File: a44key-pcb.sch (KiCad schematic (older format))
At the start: 60 parts

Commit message: Submodules added
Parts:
- C1, C2, C3, C4, C5, C6, C7: renamed from C?; footprint (none) -> Capacitor_SMD:C_0805_2012Metric
- D1, D10, D11, D12, D13, D14, D15, D16, D17, D18, D19, D2, D20, D21, D22, D3, D4, D5, D6, D7, D8, D9: renamed from D?; footprint (none) -> MX_Alps_Hybrid:MX-1U-NoLED
- F1: renamed from F?; footprint (none) -> MX_Alps_Hybrid:MX-1U-NoLED
- MX1, MX10, MX11, MX12, MX13, MX14, MX15, MX16, MX17, MX18, MX19, MX2, MX20, MX21, MX22, MX3, MX4, MX5, MX6, MX7, MX8, MX9: renamed from MX?; footprint (none) -> MX_Alps_Hybrid:MX-1U-NoLED
- R1, R2, R3, R4: renamed from R?; footprint (none) -> Resistor_SMD:R_0805_2012Metric
- SW1: renamed from SW?; footprint (none) -> random-keyboard-parts:SKQG-1155865
- USB1: renamed from USB?; footprint (none) -> random-keyboard-parts:Molex-0548190589
- Y1: renamed from Y?; footprint (none) -> Crystal:Crystal_SMD_3225-4Pin_3.2x2.5mm_HandSoldering
- gave numbers to parts that had none: 1

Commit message: Submodules added
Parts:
- added J1: AudioJack3, Connector_Audio:Jack_3.5mm_CUI_SJ1-3535NG_Horizontal, symbol Connector:AudioJack3
- D1, D10, D11, D12, D13, D14, D15, D16, D17, D18, D19, D2, D20, D21, D22, D3, D4, D5, D6, D7, D8, D9: footprint MX_Alps_Hybrid:MX-1U-NoLED -> Diode_SMD:D_SOD-123
- F1: footprint MX_Alps_Hybrid:MX-1U-NoLED -> Fuse:Fuse_1206_3216Metric
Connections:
- net GND: now also U1.15 (GND), U1.23 (GND), U1.35 (GND), U1.43 (GND)
- new net R: J1.R
- new net S: J1.S
- new net T: J1.T
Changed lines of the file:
@@
 F 0 "F1" V 6075 1200 50  0000 C CNN
 F 1 "Polyfuse" V 6166 1200 50  0000 C CNN
-F 2 "MX_Alps_Hybrid:MX-1U-NoLED" H 6350 1000 50  0001 L CNN
+F 2 "Fuse:Fuse_1206_3216Metric" H 6350 1000 50  0001 L CNN
 F 3 "~" H 6300 1200 50  0001 C CNN
 	1    6300 1200
@@
 F 0 "D1" V 6596 2532 50  0000 R CNN
 F 1 "D_Small" V 6505 2532 50  0000 R CNN
-F 2 "MX_Alps_Hybrid:MX-1U-NoLED" V 6550 2600 50  0001 C CNN
+F 2 "Diode_SMD:D_SOD-123" V 6550 2600 50  0001 C CNN
 F 3 "~" V 6550 2600 50  0001 C CNN
 	1    6550 2600
@@
 F 0 "D5" V 7296 2532 50  0000 R CNN
 F 1 "D_Small" V 7205 2532 50  0000 R CNN
-F 2 "MX_Alps_Hybrid:MX-1U-NoLED" V 7250 2600 50  0001 C CNN
+F 2 "Diode_SMD:D_SOD-123" V 7250 2600 50  0001 C CNN
 F 3 "~" V 7250 2600 50  0001 C CNN
 	1    7250 2600
@@
 F 0 "D2" V 6596 3332 50  0000 R CNN
 F 1 "D_Small" V 6505 3332 50  0000 R CNN
-F 2 "MX_Alps_Hybrid:MX-1U-NoLED" V 6550 3400 50  0001 C CNN
+F 2 "Diode_SMD:D_SOD-123" V 6550 3400 50  0001 C CNN
 F 3 "~" V 6550 3400 50  0001 C CNN
 	1    6550 3400
@@
 F 0 "D6" V 7296 3332 50  0000 R CNN
 F 1 "D_Small" V 7205 3332 50  0000 R CNN
-F 2 "MX_Alps_Hybrid:MX-1U-NoLED" V 7250 3400 50  0001 C CNN
+F 2 "Diode_SMD:D_SOD-123" V 7250 3400 50  0001 C CNN
 F 3 "~" V 7250 3400 50  0001 C CNN
 	1    7250 3400
@@
 F 0 "D9" V 7996 2532 50  0000 R CNN
 F 1 "D_Small" V 7905 2532 50  0000 R CNN
-F 2 "MX_Alps_Hybrid:MX-1U-NoLED" V 7950 2600 50  0001 C CNN
+F 2 "Diode_SMD:D_SOD-123" V 7950 2600 50  0001 C CNN
 F 3 "~" V 7950 2600 50  0001 C CNN
 	1    7950 2600
@@
 F 0 "D13" V 8696 2532 50  0000 R CNN
 F 1 "D_Small" V 8605 2532 50  0000 R CNN
-F 2 "MX_Alps_Hybrid:MX-1U-NoLED" V 8650 2600 50  0001 C CNN
+F 2 "Diode_SMD:D_SOD-123" V 8650 2600 50  0001 C CNN
 F 3 "~" V 8650 2600 50  0001 C CNN
 	1    8650 2600
@@
 F 0 "D10" V 7996 3332 50  0000 R CNN
 F 1 "D_Small" V 7905 3332 50  0000 R CNN
-F 2 "MX_Alps_Hybrid:MX-1U-NoLED" V 7950 3400 50  0001 C CNN
+F 2 "Diode_SMD:D_SOD-123" V 7950 3400 50  0001 C CNN
 F 3 "~" V 7950 3400 50  0001 C CNN
 	1    7950 3400
@@
 F 0 "D14" V 8696 3332 50  0000 R CNN
 F 1 "D_Small" V 8605 3332 50  0000 R CNN
-F 2 "MX_Alps_Hybrid:MX-1U-NoLED" V 8650 3400 50  0001 C CNN
+F 2 "Diode_SMD:D_SOD-123" V 8650 3400 50  0001 C CNN
 F 3 "~" V 8650 3400 50  0001 C CNN
 	1    8650 3400
@@
 F 0 "D3" V 6596 4132 50  0000 R CNN
 F 1 "D_Small" V 6505 4132 50  0000 R CNN
-F 2 "MX_Alps_Hybrid:MX-1U-NoLED" V 6550 4200 50  0001 C CNN
+F 2 "Diode_SMD:D_SOD-123" V 6550 4200 50  0001 C CNN
 F 3 "~" V 6550 4200 50  0001 C CNN
 	1    6550 4200
@@
 F 0 "D7" V 7296 4132 50  0000 R CNN
 F 1 "D_Small" V 7205 4132 50  0000 R CNN
-F 2 "MX_Alps_Hybrid:MX-1U-NoLED" V 7250 4200 50  0001 C CNN
+F 2 "Diode_SMD:D_SOD-123" V 7250 4200 50  0001 C CNN
 F 3 "~" V 7250 4200 50  0001 C CNN
 	1    7250 4200
@@
 F 0 "D4" V 6596 4932 50  0000 R CNN
 F 1 "D_Small" V 6505 4932 50  0000 R CNN
-F 2 "MX_Alps_Hybrid:MX-1U-NoLED" V 6550 5000 50  0001 C CNN
+F 2 "Diode_SMD:D_SOD-123" V 6550 5000 50  0001 C CNN
 F 3 "~" V 6550 5000 50  0001 C CNN
 	1    6550 5000
@@
 F 0 "D8" V 7296 4932 50  0000 R CNN
 F 1 "D_Small" V 7205 4932 50  0000 R CNN
-F 2 "MX_Alps_Hybrid:MX-1U-NoLED" V 7250 5000 50  0001 C CNN
+F 2 "Diode_SMD:D_SOD-123" V 7250 5000 50  0001 C CNN
 F 3 "~" V 7250 5000 50  0001 C CNN
 	1    7250 5000
@@
 F 0 "D11" V 7996 4132 50  0000 R CNN
 F 1 "D_Small" V 7905 4132 50  0000 R CNN
-F 2 "MX_Alps_Hybrid:MX-1U-NoLED" V 7950 4200 50  0001 C CNN
+F 2 "Diode_SMD:D_SOD-123" V 7950 4200 50  0001 C CNN
 F 3 "~" V 7950 4200 50  0001 C CNN
 	1    7950 4200
@@
 F 0 "D15" V 8696 4132 50  0000 R CNN
 F 1 "D_Small" V 8605 4132 50  0000 R CNN
-F 2 "MX_Alps_Hybrid:MX-1U-NoLED" V 8650 4200 50  0001 C CNN
+F 2 "Diode_SMD:D_SOD-123" V 8650 4200 50  0001 C CNN
 F 3 "~" V 8650 4200 50  0001 C CNN
 	1    8650 4200
@@
 F 0 "D12" V 7996 4932 50  0000 R CNN
 F 1 "D_Small" V 7905 4932 50  0000 R CNN
-F 2 "MX_Alps_Hybrid:MX-1U-NoLED" V 7950 5000 50  0001 C CNN
+F 2 "Diode_SMD:D_SOD-123" V 7950 5000 50  0001 C CNN
 F 3 "~" V 7950 5000 50  0001 C CNN
 	1    7950 5000
@@
 F 0 "D16" V 8696 4932 50  0000 R CNN
 F 1 "D_Small" V 8605 4932 50  0000 R CNN
-F 2 "MX_Alps_Hybrid:MX-1U-NoLED" V 8650 5000 50  0001 C CNN
+F 2 "Diode_SMD:D_SOD-123" V 8650 5000 50  0001 C CNN
 F 3 "~" V 8650 5000 50  0001 C CNN
 	1    8650 5000
@@
 F 0 "D17" V 9346 2532 50  0000 R CNN
 F 1 "D_Small" V 9255 2532 50  0000 R CNN
-F 2 "MX_Alps_Hybrid:MX-1U-NoLED" V 9300 2600 50  0001 C CNN
+F 2 "Diode_SMD:D_SOD-123" V 9300 2600 50  0001 C CNN
 F 3 "~" V 9300 2600 50  0001 C CNN
 	1    9300 2600
@@
 F 0 "D20" V 10046 2532 50  0000 R CNN
 F 1 "D_Small" V 9955 2532 50  0000 R CNN
-F 2 "MX_Alps_Hybrid:MX-1U-NoLED" V 10000 2600 50  0001 C CNN
+F 2 "Diode_SMD:D_SOD-123" V 10000 2600 50  0001 C CNN
 F 3 "~" V 10000 2600 50  0001 C CNN
 	1    10000 2600
@@
 F 0 "D18" V 9346 3332 50  0000 R CNN
 F 1 "D_Small" V 9255 3332 50  0000 R CNN
-F 2 "MX_Alps_Hybrid:MX-1U-NoLED" V 9300 3400 50  0001 C CNN
+F 2 "Diode_SMD:D_SOD-123" V 9300 3400 50  0001 C CNN
 F 3 "~" V 9300 3400 50  0001 C CNN
 	1    9300 3400
@@
 F 0 "D21" V 10046 3332 50  0000 R CNN
 F 1 "D_Small" V 9955 3332 50  0000 R CNN
-F 2 "MX_Alps_Hybrid:MX-1U-NoLED" V 10000 3400 50  0001 C CNN
+F 2 "Diode_SMD:D_SOD-123" V 10000 3400 50  0001 C CNN
 F 3 "~" V 10000 3400 50  0001 C CNN
 	1    10000 3400
@@
 F 0 "D19" V 9346 4132 50  0000 R CNN
 F 1 "D_Small" V 9255 4132 50  0000 R CNN
-F 2 "MX_Alps_Hybrid:MX-1U-NoLED" V 9300 4200 50  0001 C CNN
+F 2 "Diode_SMD:D_SOD-123" V 9300 4200 50  0001 C CNN
 F 3 "~" V 9300 4200 50  0001 C CNN
 	1    9300 4200
@@
 F 0 "D22" V 10046 4132 50  0000 R CNN
 F 1 "D_Small" V 9955 4132 50  0000 R CNN
-F 2 "MX_Alps_Hybrid:MX-1U-NoLED" V 10000 4200 50  0001 C CNN
+F 2 "Diode_SMD:D_SOD-123" V 10000 4200 50  0001 C CNN
 F 3 "~" V 10000 4200 50  0001 C CNN
 	1    10000 4200
@@
 Text GLabel 6200 5100 0    50   Input ~ 0
 ROW3
+$Comp
+L Connector:AudioJack3 J1
+U 1 1 6186D5DF
+P 4800 2950
+F 0 "J1" H 4782 3275 50  0000 C CNN
+F 1 "AudioJack3" H 4782 3184 50  0000 C CNN
+F 2 "Connector_Audio:Jack_3.5mm_CUI_SJ1-3535NG_Horizontal" H 4800 2950 50  0001 C CNN
+F 3 "~" H 4800 2950 50  0001 C CNN
+	1    4800 2950
+	1    0    0    -1
+$EndComp
+Text GLabel 5000 2850 2    50   Input ~ 0
+S
+Text GLabel 5000 2950 2    50   Input ~ 0
+R
+Text GLabel 5000 3050 2    50   Input ~ 0
+T
+Wire Wire Line
+	3500 5550 3600 5550
+Connection ~ 3500 5550
 $EndSCHEMATC

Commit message: Submodules added
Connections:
- net +5V: now also U1.24 (AVCC), U1.44 (AVCC)
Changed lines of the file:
@@
 Wire Wire Line
 	3000 3050 2700 3050
-Wire Wire Line
-	2700 3050 2700 2950
-Connection ~ 2700 2950
-Wire Wire Line
-	2700 2950 2700 2800
 $Comp
 L Device:Crystal_GND24_Small Y1
@@
 	3500 5550 3600 5550
 Connection ~ 3500 5550
+Wire Wire Line
+	3700 1950 3600 1950
+Connection ~ 3600 1950
+Wire Wire Line
+	2700 3050 2700 2950
 $EndSCHEMATC

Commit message: Somewhat ready
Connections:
- net R is gone; now on net SCL: J1.R
- net S is gone; now on net GND: J1.S
- net T is gone; now on net +5V: J1.T
- net VCC is gone; now on net +5V: F1.2, USB1.5 (VBUS)
- net SCL: now reaches U1.18 (PD0)
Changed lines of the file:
@@
 	1    0    0    -1
 $EndComp
-Text GLabel 5000 2850 2    50   Input ~ 0
-S
 Text GLabel 5000 2950 2    50   Input ~ 0
-R
+SCL
 Text GLabel 5000 3050 2    50   Input ~ 0
-T
+VCC
 Wire Wire Line
 	3500 5550 3600 5550
@@
 Wire Wire Line
 	2700 3050 2700 2950
+Text GLabel 4200 3450 2    50   Input ~ 0
+SCL
+Text GLabel 3600 1950 1    50   Input ~ 0
+VCC
+$Comp
+L power:GND #PWR?
+U 1 1 619786D4
+P 5300 2850
+F 0 "#PWR?" H 5300 2600 50  0001 C CNN
+F 1 "GND" H 5305 2677 50  0000 C CNN
+F 2 "" H 5300 2850 50  0001 C CNN
+F 3 "" H 5300 2850 50  0001 C CNN
+	1    5300 2850
+	1    0    0    -1
+$EndComp
+Wire Wire Line
+	5000 2850 5300 2850
 $EndSCHEMATC

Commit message: Rewired
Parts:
- J1: footprint Connector_Audio:Jack_3.5mm_CUI_SJ1-3535NG_Horizontal -> SJ-43514:CUI_SJ-43514; symbol Connector:AudioJack3 -> SJ-43514:SJ-43514
- MX1, MX10, MX11, MX12, MX13, MX14, MX15, MX16, MX17, MX18, MX19, MX2, MX20, MX21, MX22, MX3, MX4, MX5, MX6, MX7, MX8, MX9: footprint MX_Alps_Hybrid:MX-1U-NoLED -> MX_Alps_Hybrid:MX-Alps-Choc-X-1U-NoLED
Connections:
- net +5V: now also J1.2; no longer J1.T
- net COL0: now also U1.37 (PF6)
- net COL1: now also U1.36 (PF7)
- net COL2: now also U1.9 (PB1)
- net COL3: now also U1.11 (PB3)
- net COL4: now also U1.10 (PB2)
- net COL5: now also U1.30 (PB6)
- net GND: now also J1.1; no longer J1.S
- net ROW0: now also U1.27 (PD7)
- net ROW1: now also U1.1 (PE6)
- net ROW2: now also U1.28 (PB4)
- net ROW3: now also U1.29 (PB5)
- net SCL: now also J1.3; no longer J1.R
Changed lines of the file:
@@
 EESchema Schematic File Version 4
+LIBS:a44key-pcb-cache
 EELAYER 30 0
 EELAYER END
@@
 F 0 "MX1" H 6733 2573 60  0000 C CNN
 F 1 "MX-NoLED" H 6733 2499 20  0000 C CNN
-F 2 "MX_Alps_Hybrid:MX-1U-NoLED" H 6075 2325 60  0001 C CNN
+F 2 "MX_Alps_Hybrid:MX-Alps-Choc-X-1U-NoLED" H 6075 2325 60  0001 C CNN
 F 3 "" H 6075 2325 60  0001 C CNN
 	1    6700 2350
@@
 F 0 "MX5" H 7433 2573 60  0000 C CNN
 F 1 "MX-NoLED" H 7433 2499 20  0000 C CNN
-F 2 "MX_Alps_Hybrid:MX-1U-NoLED" H 6775 2325 60  0001 C CNN
+F 2 "MX_Alps_Hybrid:MX-Alps-Choc-X-1U-NoLED" H 6775 2325 60  0001 C CNN
 F 3 "" H 6775 2325 60  0001 C CNN
 	1    7400 2350
@@
 F 0 "MX2" H 6733 3373 60  0000 C CNN
 F 1 "MX-NoLED" H 6733 3299 20  0000 C CNN
-F 2 "MX_Alps_Hybrid:MX-1U-NoLED" H 6075 3125 60  0001 C CNN
+F 2 "MX_Alps_Hybrid:MX-Alps-Choc-X-1U-NoLED" H 6075 3125 60  0001 C CNN
 F 3 "" H 6075 3125 60  0001 C CNN
 	1    6700 3150
@@
 F 0 "MX6" H 7433 3373 60  0000 C CNN
 F 1 "MX-NoLED" H 7433 3299 20  0000 C CNN
-F 2 "MX_Alps_Hybrid:MX-1U-NoLED" H 6775 3125 60  0001 C CNN
+F 2 "MX_Alps_Hybrid:MX-Alps-Choc-X-1U-NoLED" H 6775 3125 60  0001 C CNN
 F 3 "" H 6775 3125 60  0001 C CNN
 	1    7400 3150
@@
 F 0 "MX9" H 8133 2573 60  0000 C CNN
 F 1 "MX-NoLED" H 8133 2499 20  0000 C CNN
-F 2 "MX_Alps_Hybrid:MX-1U-NoLED" H 7475 2325 60  0001 C CNN
+F 2 "MX_Alps_Hybrid:MX-Alps-Choc-X-1U-NoLED" H 7475 2325 60  0001 C CNN
 F 3 "" H 7475 2325 60  0001 C CNN
 	1    8100 2350
@@
 F 0 "MX13" H 8833 2573 60  0000 C CNN
 F 1 "MX-NoLED" H 8833 2499 20  0000 C CNN
-F 2 "MX_Alps_Hybrid:MX-1U-NoLED" H 8175 2325 60  0001 C CNN
+F 2 "MX_Alps_Hybrid:MX-Alps-Choc-X-1U-NoLED" H 8175 2325 60  0001 C CNN
 F 3 "" H 8175 2325 60  0001 C CNN
 	1    8800 2350
@@
 F 0 "MX10" H 8133 3373 60  0000 C CNN
 F 1 "MX-NoLED" H 8133 3299 20  0000 C CNN
-F 2 "MX_Alps_Hybrid:MX-1U-NoLED" H 7475 3125 60  0001 C CNN
+F 2 "MX_Alps_Hybrid:MX-Alps-Choc-X-1U-NoLED" H 7475 3125 60  0001 C CNN
 F 3 "" H 7475 3125 60  0001 C CNN
 	1    8100 3150
@@
 F 0 "MX14" H 8833 3373 60  0000 C CNN
 F 1 "MX-NoLED" H 8833 3299 20  0000 C CNN
-F 2 "MX_Alps_Hybrid:MX-1U-NoLED" H 8175 3125 60  0001 C CNN
+F 2 "MX_Alps_Hybrid:MX-Alps-Choc-X-1U-NoLED" H 8175 3125 60  0001 C CNN
 F 3 "" H 8175 3125 60  0001 C CNN
 	1    8800 3150
@@
 F 0 "MX3" H 6733 4173 60  0000 C CNN
 F 1 "MX-NoLED" H 6733 4099 20  0000 C CNN
-F 2 "MX_Alps_Hybrid:MX-1U-NoLED" H 6075 3925 60  0001 C CNN
+F 2 "MX_Alps_Hybrid:MX-Alps-Choc-X-1U-NoLED" H 6075 3925 60  0001 C CNN
 F 3 "" H 6075 3925 60  0001 C CNN
 	1    6700 3950
@@
 F 0 "MX7" H 7433 4173 60  0000 C CNN
 F 1 "MX-NoLED" H 7433 4099 20  0000 C CNN
-F 2 "MX_Alps_Hybrid:MX-1U-NoLED" H 6775 3925 60  0001 C CNN
+F 2 "MX_Alps_Hybrid:MX-Alps-Choc-X-1U-NoLED" H 6775 3925 60  0001 C CNN
 F 3 "" H 6775 3925 60  0001 C CNN
 	1    7400 3950
@@
 F 0 "MX4" H 6733 4973 60  0000 C CNN
 F 1 "MX-NoLED" H 6733 4899 20  0000 C CNN
-F 2 "MX_Alps_Hybrid:MX-1U-NoLED" H 6075 4725 60  0001 C CNN
+F 2 "MX_Alps_Hybrid:MX-Alps-Choc-X-1U-NoLED" H 6075 4725 60  0001 C CNN
 F 3 "" H 6075 4725 60  0001 C CNN
 	1    6700 4750
@@
 F 0 "MX8" H 7433 4973 60  0000 C CNN
 F 1 "MX-NoLED" H 7433 4899 20  0000 C CNN
-F 2 "MX_Alps_Hybrid:MX-1U-NoLED" H 6775 4725 60  0001 C CNN
+F 2 "MX_Alps_Hybrid:MX-Alps-Choc-X-1U-NoLED" H 6775 4725 60  0001 C CNN
 F 3 "" H 6775 4725 60  0001 C CNN
 	1    7400 4750
@@
 F 0 "MX11" H 8133 4173 60  0000 C CNN
 F 1 "MX-NoLED" H 8133 4099 20  0000 C CNN
-F 2 "MX_Alps_Hybrid:MX-1U-NoLED" H 7475 3925 60  0001 C CNN
+F 2 "MX_Alps_Hybrid:MX-Alps-Choc-X-1U-NoLED" H 7475 3925 60  0001 C CNN
 F 3 "" H 7475 3925 60  0001 C CNN
 	1    8100 3950
@@
 F 0 "MX15" H 8833 4173 60  0000 C CNN
 F 1 "MX-NoLED" H 8833 4099 20  0000 C CNN
-F 2 "MX_Alps_Hybrid:MX-1U-NoLED" H 8175 3925 60  0001 C CNN
+F 2 "MX_Alps_Hybrid:MX-Alps-Choc-X-1U-NoLED" H 8175 3925 60  0001 C CNN
 F 3 "" H 8175 3925 60  0001 C CNN
 	1    8800 3950
@@
 F 0 "MX12" H 8133 4973 60  0000 C CNN
 F 1 "MX-NoLED" H 8133 4899 20  0000 C CNN
-F 2 "MX_Alps_Hybrid:MX-1U-NoLED" H 7475 4725 60  0001 C CNN
+F 2 "MX_Alps_Hybrid:MX-Alps-Choc-X-1U-NoLED" H 7475 4725 60  0001 C CNN
 F 3 "" H 7475 4725 60  0001 C CNN
 	1    8100 4750
@@
 F 0 "MX16" H 8833 4973 60  0000 C CNN
 F 1 "MX-NoLED" H 8833 4899 20  0000 C CNN
-F 2 "MX_Alps_Hybrid:MX-1U-NoLED" H 8175 4725 60  0001 C CNN
+F 2 "MX_Alps_Hybrid:MX-Alps-Choc-X-1U-NoLED" H 8175 4725 60  0001 C CNN
 F 3 "" H 8175 4725 60  0001 C CNN
 	1    8800 4750
@@
 F 0 "MX17" H 9483 2573 60  0000 C CNN
 F 1 "MX-NoLED" H 9483 2499 20  0000 C CNN
-F 2 "MX_Alps_Hybrid:MX-1U-NoLED" H 8825 2325 60  0001 C CNN
+F 2 "MX_Alps_Hybrid:MX-Alps-Choc-X-1U-NoLED" H 8825 2325 60  0001 C CNN
 F 3 "" H 8825 2325 60  0001 C CNN
 	1    9450 2350
@@
 F 0 "MX20" H 10183 2573 60  0000 C CNN
 F 1 "MX-NoLED" H 10183 2499 20  0000 C CNN
-F 2 "MX_Alps_Hybrid:MX-1U-NoLED" H 9525 2325 60  0001 C CNN
+F 2 "MX_Alps_Hybrid:MX-Alps-Choc-X-1U-NoLED" H 9525 2325 60  0001 C CNN
 F 3 "" H 9525 2325 60  0001 C CNN
 	1    10150 2350
@@
 F 0 "MX18" H 9483 3373 60  0000 C CNN
 F 1 "MX-NoLED" H 9483 3299 20  0000 C CNN
-F 2 "MX_Alps_Hybrid:MX-1U-NoLED" H 8825 3125 60  0001 C CNN
+F 2 "MX_Alps_Hybrid:MX-Alps-Choc-X-1U-NoLED" H 8825 3125 60  0001 C CNN
 F 3 "" H 8825 3125 60  0001 C CNN
 	1    9450 3150
@@
 F 0 "MX21" H 10183 3373 60  0000 C CNN
 F 1 "MX-NoLED" H 10183 3299 20  0000 C CNN
-F 2 "MX_Alps_Hybrid:MX-1U-NoLED" H 9525 3125 60  0001 C CNN
+F 2 "MX_Alps_Hybrid:MX-Alps-Choc-X-1U-NoLED" H 9525 3125 60  0001 C CNN
 F 3 "" H 9525 3125 60  0001 C CNN
 	1    10150 3150
@@
 F 0 "MX19" H 9483 4173 60  0000 C CNN
 F 1 "MX-NoLED" H 9483 4099 20  0000 C CNN
-F 2 "MX_Alps_Hybrid:MX-1U-NoLED" H 8825 3925 60  0001 C CNN
+F 2 "MX_Alps_Hybrid:MX-Alps-Choc-X-1U-NoLED" H 8825 3925 60  0001 C CNN
 F 3 "" H 8825 3925 60  0001 C CNN
 	1    9450 3950
@@
 F 0 "MX22" H 10183 4173 60  0000 C CNN
 F 1 "MX-NoLED" H 10183 4099 20  0000 C CNN
-F 2 "MX_Alps_Hybrid:MX-1U-NoLED" H 9525 3925 60  0001 C CNN
+F 2 "MX_Alps_Hybrid:MX-Alps-Choc-X-1U-NoLED" H 9525 3925 60  0001 C CNN
 F 3 "" H 9525 3925 60  0001 C CNN
 	1    10150 3950
@@
 ROW3
 $Comp
-L Connector:AudioJack3 J1
+L SJ-43514:SJ-43514 J1
 U 1 1 6186D5DF
-P 4800 2950
-F 0 "J1" H 4782 3275 50  0000 C CNN
-F 1 "AudioJack3" H 4782 3184 50  0000 C CNN
-F 2 "Connector_Audio:Jack_3.5mm_CUI_SJ1-3535NG_Horizontal" H 4800 2950 50  0001 C CNN
-F 3 "~" H 4800 2950 50  0001 C CNN
-	1    4800 2950
-	1    0    0    -1
-$EndComp
-Text GLabel 5000 2950 2    50   Input ~ 0
-SCL
-Text GLabel 5000 3050 2    50   Input ~ 0
+P 3850 850
+F 0 "J1" H 3832 1175 50  0000 C CNN
+F 1 "AudioJack3" H 3832 1084 50  0000 C CNN
+F 2 "SJ-43514:CUI_SJ-43514" H 3850 850 50  0001 C CNN
+F 3 "~" H 3850 850 50  0001 C CNN
+	1    3850 850
+	1    0    0    -1
+$EndComp
+Text GLabel 4250 750  2    50   Input ~ 0
 VCC
 Wire Wire Line
@@
 VCC
 $Comp
-L power:GND #PWR?
+L power:GND #PWR0114
 U 1 1 619786D4
-P 5300 2850
-F 0 "#PWR?" H 5300 2600 50  0001 C CNN
-F 1 "GND" H 5305 2677 50  0000 C CNN
-F 2 "" H 5300 2850 50  0001 C CNN
-F 3 "" H 5300 2850 50  0001 C CNN
-	1    5300 2850
-	1    0    0    -1
-$EndComp
-Wire Wire Line
-	5000 2850 5300 2850
+P 4500 1050
+F 0 "#PWR0114" H 4500 800 50  0001 C CNN
+F 1 "GND" H 4505 877 50  0000 C CNN
+F 2 "" H 4500 1050 50  0001 C CNN
+F 3 "" H 4500 1050 50  0001 C CNN
+	1    4500 1050
+	1    0    0    -1
+$EndComp
+Wire Wire Line
+	4250 1050 4500 1050
+Text GLabel 4250 950  2    50   Input ~ 0
+SCL
+Text GLabel 4200 4150 2    50   Input ~ 0
+ROW0
+Text GLabel 4200 4450 2    50   Input ~ 0
+ROW1
+Text GLabel 4200 2650 2    50   Input ~ 0
+ROW2
+Text GLabel 4200 2750 2    50   Input ~ 0
+ROW3
+Text GLabel 4200 5050 2    50   Input ~ 0
+COL0
+Text GLabel 4200 5150 2    50   Input ~ 0
+COL1
+Text GLabel 4200 2350 2    50   Input ~ 0
+COL2
+Text GLabel 4200 2550 2    50   Input ~ 0
+COL3
+Text GLabel 4200 2450 2    50   Input ~ 0
+COL4
+Text GLabel 4200 2850 2    50   Input ~ 0
+COL5
 $EndSCHEMATC

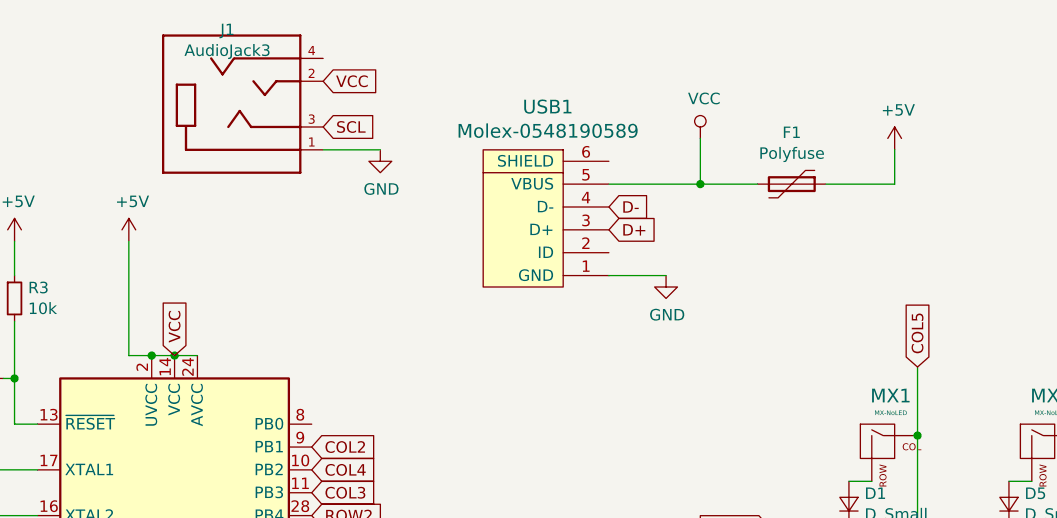
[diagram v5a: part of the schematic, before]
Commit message: Covered with zones
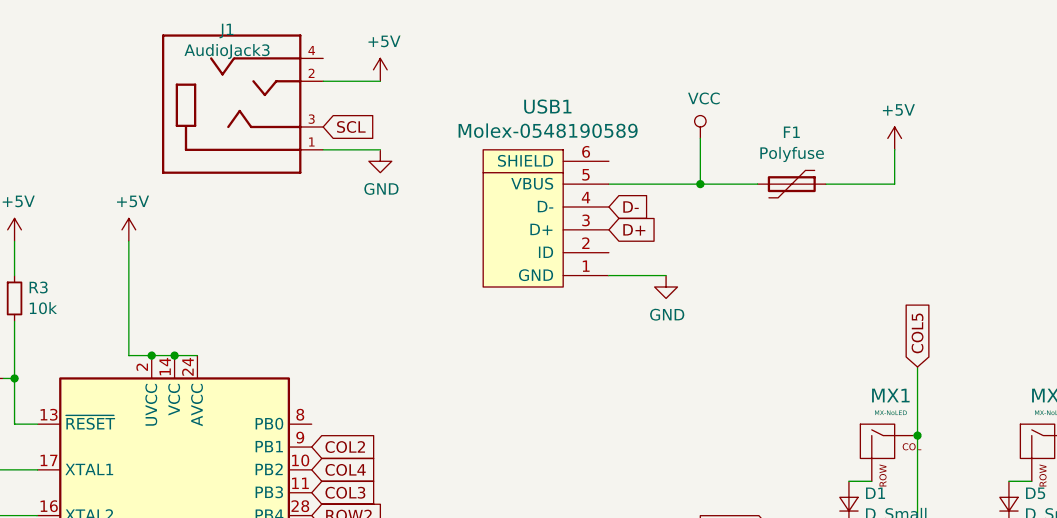
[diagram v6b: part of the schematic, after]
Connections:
- net +5V: no longer F1.2, USB1.5 (VBUS)
- new net VCC: F1.2, USB1.5 (VBUS)
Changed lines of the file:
@@
 	0    -1   -1   0
-$EndComp
-$Comp
-L Device:Polyfuse F1
-U 1 1 616D8C6B
-P 6300 1200
-F 0 "F1" V 6075 1200 50  0000 C CNN
-F 1 "Polyfuse" V 6166 1200 50  0000 C CNN
-F 2 "Fuse:Fuse_1206_3216Metric" H 6350 1000 50  0001 L CNN
-F 3 "~" H 6300 1200 50  0001 C CNN
-	1    6300 1200
-	0    1    1    0
 $EndComp
 Wire Wire Line
@@
 Wire Wire Line
 	6750 1050 6750 1200
-Wire Wire Line
-	6750 1200 6450 1200
 $Comp
 L power:GND #PWR0113
@@
 	1    0    0    -1
 $EndComp
-Text GLabel 4250 750  2    50   Input ~ 0
-VCC
 Wire Wire Line
 	3500 5550 3600 5550
@@
 Text GLabel 4200 3450 2    50   Input ~ 0
 SCL
-Text GLabel 3600 1950 1    50   Input ~ 0
-VCC
 $Comp
 L power:GND #PWR0114
@@
 Text GLabel 4200 2850 2    50   Input ~ 0
 COL5
+$Comp
+L Device:Polyfuse F1
+U 1 1 616D8C6B
+P 6300 1200
+F 0 "F1" V 6075 1200 50  0000 C CNN
+F 1 "Polyfuse" V 6166 1200 50  0000 C CNN
+F 2 "Fuse:Fuse_1206_3216Metric" H 6350 1000 50  0001 L CNN
+F 3 "~" H 6300 1200 50  0001 C CNN
+	1    6300 1200
+	0    1    1    0
+$EndComp
+Wire Wire Line
+	6450 1200 6750 1200
+$Comp
+L power:+5V #PWR?
+U 1 1 617476F1
+P 4500 750
+F 0 "#PWR?" H 4500 600 50  0001 C CNN
+F 1 "+5V" H 4515 923 50  0000 C CNN
+F 2 "" H 4500 750 50  0001 C CNN
+F 3 "" H 4500 750 50  0001 C CNN
+	1    4500 750
+	1    0    0    -1
+$EndComp
+Wire Wire Line
+	4250 750  4500 750
 $EndSCHEMATC
